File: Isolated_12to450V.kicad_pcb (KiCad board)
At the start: 4 copper layers, 85 x 47.5 mm, 76 parts, among them J1 Screw_Terminal_01x04, J20 T44007, J21 T44007, Q1 HY1707, Q20 BC817, Q21 SUD50P06-15, U1 UC3845, U20 TCMT1108, U21 TL431M

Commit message: Update Outputs (release)
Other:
- board text added: "0.001mm"
- board text added: "0.035mm (1.00oz)"
- board text added: "1.35mm"
- board text added: "Copper Layer"
- board text added: "FR4"
- board text added: "L1 (Ref)"
- board text added: "Plane"
- board text added: "Prepreg"
- board text added: "Total thickness: 1.602mm"
- board text added: "Virtual (Bot side jumpers)"
- board text added: "Virtual (Top side jumpers)"
- board text removed: "1.48mm"
- board text removed: "L1 (Sig, PWR)"
- board text removed: "Total thickness: 1.66mm"

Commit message: Sch update ongoing
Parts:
- removed D23: BZT52B5V1, Diode_SMD:D_SOD-123
- added C30: 220p, Capacitor_THT:C_Rect_L16.5mm_W5.0mm_P15.00mm_MKT, F.Cu at (195.3, 78.2)
- added R31: 2k2, Resistor_SMD:R_0603_1608Metric_Pad0.98x0.95mm_HandSolder, F.Cu at (213.7, 63.8)
- added R32: 0, Resistor_SMD:R_0603_1608Metric_Pad0.98x0.95mm_HandSolder, F.Cu at (213.7, 66.3)
- added R33: 0, Resistor_SMD:R_0603_1608Metric_Pad0.98x0.95mm_HandSolder, F.Cu at (213.7, 68.8)
- added R34: 470, Resistor_THT:R_Axial_DIN0918_L18.0mm_D9.0mm_P7.62mm_Vertical, F.Cu at (201.9, 67.8)
- added R35: 20m, Resistor_SMD:R_Shunt_Vishay_WSR2_WSR3, F.Cu at (149.4, 35.8)
- C20: value 6.8p -> 100n
- C21: value 22p -> 100p
- C24, C27: footprint Capacitor_SMD:C_0805_2012Metric_Pad1.18x1.45mm_HandSolder -> Capacitor_SMD:C_1206_3216Metric_Pad1.33x1.80mm_HandSolder
- C3: value 3n3 -> 1n
- C4: value 1.5n -> 1n
- R20: value 15M -> 100k
- R26: value 1k -> 4.7k
- R29: value 0 -> 1k
- R3: value 5k -> 10k
- R5: value 5k1 -> 15k
- R8: footprint Resistor_SMD:R_0603_1608Metric_Pad0.98x0.95mm_HandSolder -> Resistor_SMD:R_1206_3216Metric_Pad1.30x1.75mm_HandSolder
- R9: footprint Resistor_THT:R_Axial_DIN0309_L9.0mm_D3.2mm_P15.24mm_Horizontal -> Personal:Shunt_alixp_module
- moved R9 8.90 mm to (149.3, 49.5), turned to 0 degrees
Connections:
- C20 pad 2: /Block Diagram/Schematic/Sec_comp_mid -> /Block Diagram/Schematic/Sec_cp_m
- C21 pad 1: /Block Diagram/Schematic/Sec_comp_mid -> /Block Diagram/Schematic/Sec_ref_sns
- C25 pad 1: /Block Diagram/Schematic/OpEm -> Net-(C25-Pad1)
- R20 pad 2: /Block Diagram/Schematic/Sec_comp_mid -> /Block Diagram/Schematic/Sec_cp_m
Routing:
- net /Block Diagram/Schematic/Sec_ref_sns: track 28.1 -> 31.2 mm
- net /Block Diagram/Schematic/Sec_comp_mid: track 3.05 -> 0.00 mm

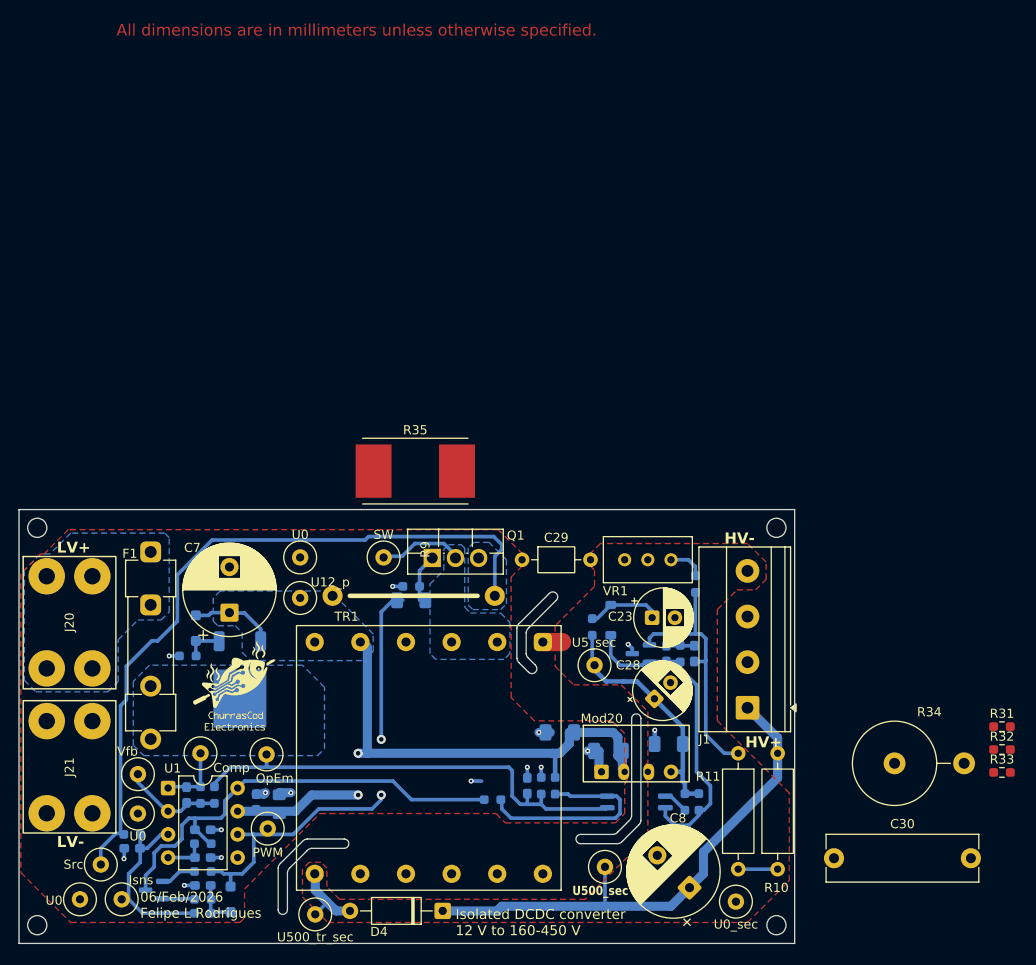
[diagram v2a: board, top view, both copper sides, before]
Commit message: Schematic nearly complete
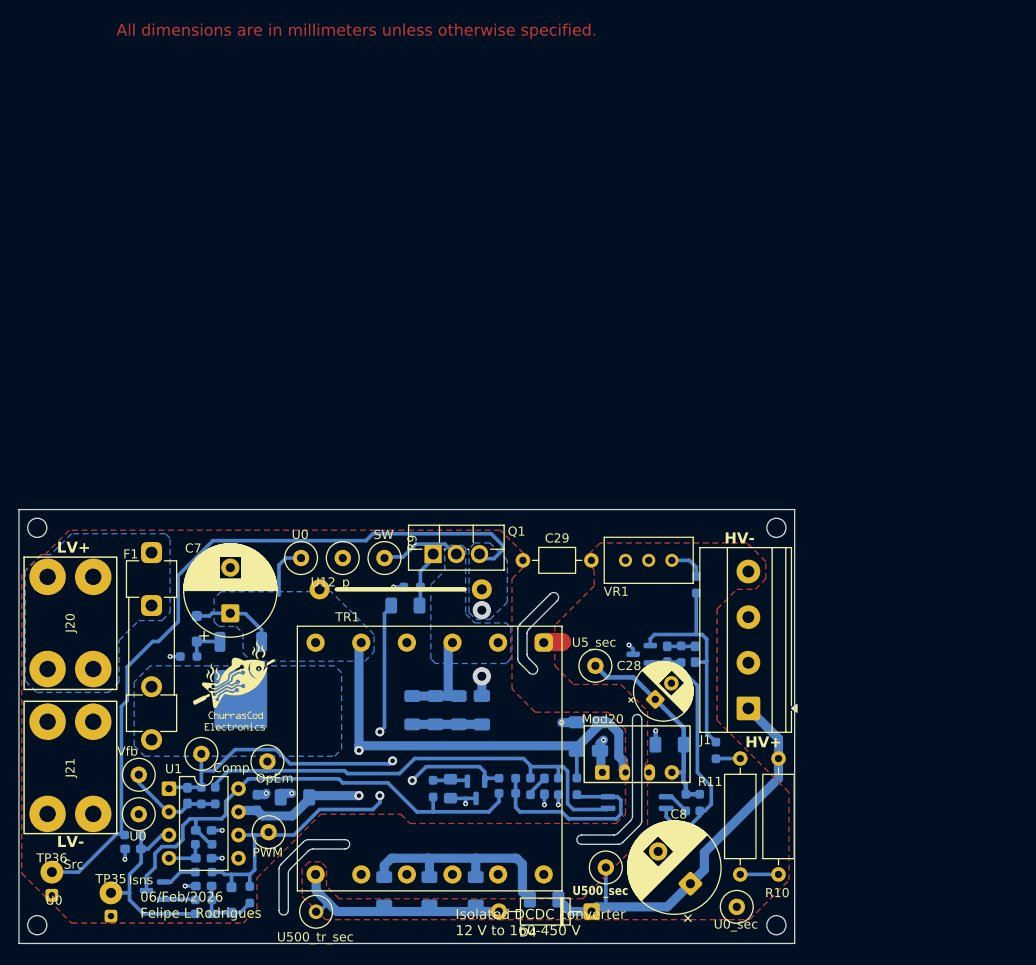
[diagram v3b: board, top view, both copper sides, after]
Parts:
- removed C23: 100u, Capacitor_THT:CP_Radial_D6.3mm_P2.50mm
- removed D21: 1N4148W, Diode_SMD:D_SOD-123
- removed R27: 15k, Resistor_SMD:R_0603_1608Metric_Pad0.98x0.95mm_HandSolder
- removed TP21, TP22, TP29: TestPoint_Alt, TestPoint:TestPoint_Loop_D3.50mm_Drill0.9mm_Beaded
- added C31: 2.7n, Capacitor_SMD:C_1206_3216Metric_Pad1.33x1.80mm_HandSolder, B.Cu at (156.7, 62.0)
- added C32: 1u, Capacitor_SMD:C_0805_2012Metric_Pad1.18x1.45mm_HandSolder, B.Cu at (153.3, 70.6)
- added Q22: BC857, Package_TO_SOT_SMD:SOT-23, B.Cu at (156.1, 70.7)
- added R36: 33, Resistor_SMD:R_1206_3216Metric_Pad1.30x1.75mm_HandSolder, B.Cu at (149.1, 62.0)
- added R37: 33, Resistor_SMD:R_1206_3216Metric_Pad1.30x1.75mm_HandSolder, B.Cu at (151.6, 62.0)
- added R38: 33, Resistor_SMD:R_1206_3216Metric_Pad1.30x1.75mm_HandSolder, B.Cu at (154.2, 62.0)
- added R39: 470, Resistor_SMD:R_1206_3216Metric_Pad1.30x1.75mm_HandSolder, B.Cu at (151.0, 81.9)
- added R40: 470, Resistor_SMD:R_1206_3216Metric_Pad1.30x1.75mm_HandSolder, B.Cu at (146.0, 81.9)
- added R41: 470, Resistor_SMD:R_1206_3216Metric_Pad1.30x1.75mm_HandSolder, B.Cu at (156.1, 81.9)
- added TP35: ~, Personal:Testpoint_osc_no_lead, F.Cu at (116.1, 83.3)
- added TP36: ~, Personal:Testpoint_osc_no_lead, F.Cu at (109.6, 81.0)
- C30: footprint Capacitor_THT:C_Rect_L16.5mm_W5.0mm_P15.00mm_MKT -> Capacitor_SMD:C_1206_3216Metric_Pad1.33x1.80mm_HandSolder; moved to B.Cu
- C6: footprint Capacitor_SMD:C_0805_2012Metric_Pad1.18x1.45mm_HandSolder -> Capacitor_SMD:C_1206_3216Metric_Pad1.33x1.80mm_HandSolder
- R23: value 1k -> 470
- R31, R32, R33: moved to B.Cu
- R34: value 470 -> 0; footprint Resistor_THT:R_Axial_DIN0918_L18.0mm_D9.0mm_P7.62mm_Vertical -> Resistor_SMD:R_0603_1608Metric_Pad0.98x0.95mm_HandSolder; moved to B.Cu
- R35: value 20m -> 100k; footprint Resistor_SMD:R_Shunt_Vishay_WSR2_WSR3 -> Resistor_SMD:R_0603_1608Metric_Pad0.98x0.95mm_HandSolder; moved to B.Cu
- moved R31 84.5 mm to (131.3, 82.2), turned to 90 degrees
- moved R33 54.2 mm to (159.5, 69.5), turned to 180 degrees
- moved R32 51.8 mm to (162.1, 70.4), turned to -90 degrees
- moved R35 34.9 mm to (151.4, 70.6), turned to 90 degrees
- moved C30 32.1 mm to (163.5, 82.7)
- moved R34 19.6 mm to (182.4, 66.4), turned to 90 degrees
- moved D4 16.3 mm to (168.8, 84.1)
- moved TP33 4.67 mm to (141.5, 45.3)
- moved TP31 4.38 mm to (136.9, 45.3)
- moved R29 2.38 mm to (167.1, 70.4)
- moved C27 1.93 mm to (167.1, 64.9), turned to 90 degrees
- moved C25 1.88 mm to (163.6, 70.4), turned to -90 degrees
- moved R12 1.88 mm to (165.1, 70.4), turned to -90 degrees
- moved C6 1.87 mm to (136.2, 71.6), turned to 180 degrees
- moved C24 1.83 mm to (169.7, 64.9), turned to -90 degrees
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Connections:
- R11 pad 1: /Block Diagram/Schematic/Sec_ref_sns -> /Block Diagram/Schematic/Sec_div_h2
- R34 pad 1: /Block Diagram/Schematic/U500_sn_sec -> /Block Diagram/Schematic/Sec_div_h2
- R34 pad 2: /Block Diagram/Schematic/U500_tr_sec -> /Block Diagram/Schematic/Sec_ref_sns
- R35 pad 1: /Block Diagram/Schematic/Src -> /Block Diagram/Schematic/U5_ref
- R35 pad 2: U0 -> Net-(Q22-B)
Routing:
- net /Block Diagram/Schematic/Comp: track 7.06 -> 44.5 mm, vias 0 -> 2
- net /Block Diagram/Schematic/U500_sn_sec: track 0.00 -> 25.4 mm
- net /Block Diagram/Schematic/U500_tr_sec: track 8.46 -> 26.6 mm
- net /Block Diagram/Schematic/U500_sec: track 57.1 -> 44.8 mm
- net /Block Diagram/Schematic/SW: track 9.35 -> 21.6 mm
- net /Block Diagram/Schematic/Src: track 79.9 -> 91.9 mm, vias 0 -> 2
- net /Block Diagram/Schematic/U12_p: track 76.7 -> 84.9 mm
- net /Block Diagram/Schematic/Sec_ss_cap: track 8.19 -> 0.00 mm
- net Net-(C31-Pad2): track 0.00 -> 7.63 mm
- net /Block Diagram/Schematic/Sec_OpK: track 35.0 -> 27.9 mm
- net /Block Diagram/Schematic/U5_ref: track 50.1 -> 55.5 mm
- net Net-(Q22-B): track 0.00 -> 3.79 mm
- net /Block Diagram/Schematic/U5_sec: track 26.4 -> 22.7 mm
- net /Block Diagram/Schematic/Sec_ref_sns: track 31.2 -> 27.9 mm
- net U0: track 18.1 -> 20.9 mm
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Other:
- outline, holes or cut-outs redrawn
